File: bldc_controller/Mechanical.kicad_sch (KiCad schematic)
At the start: 9 parts

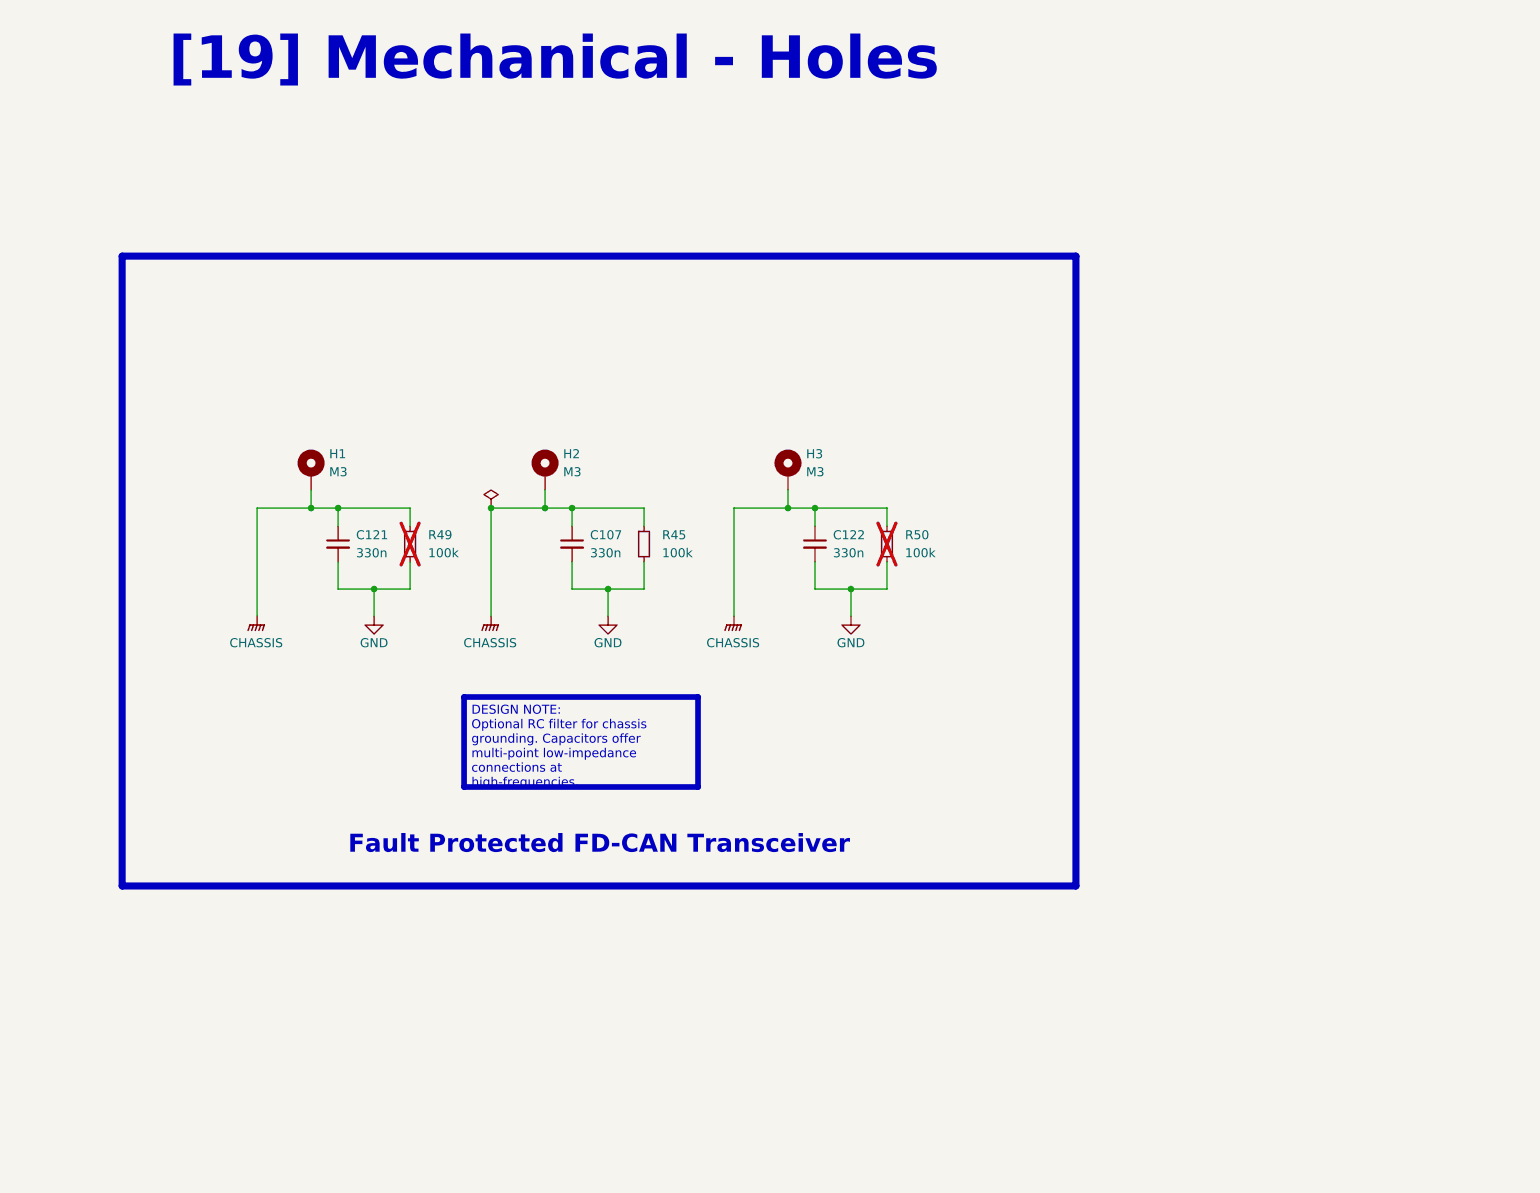
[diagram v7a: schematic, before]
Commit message: Replaced 3v3 buck with WSON package alternative. Will back-annotate components
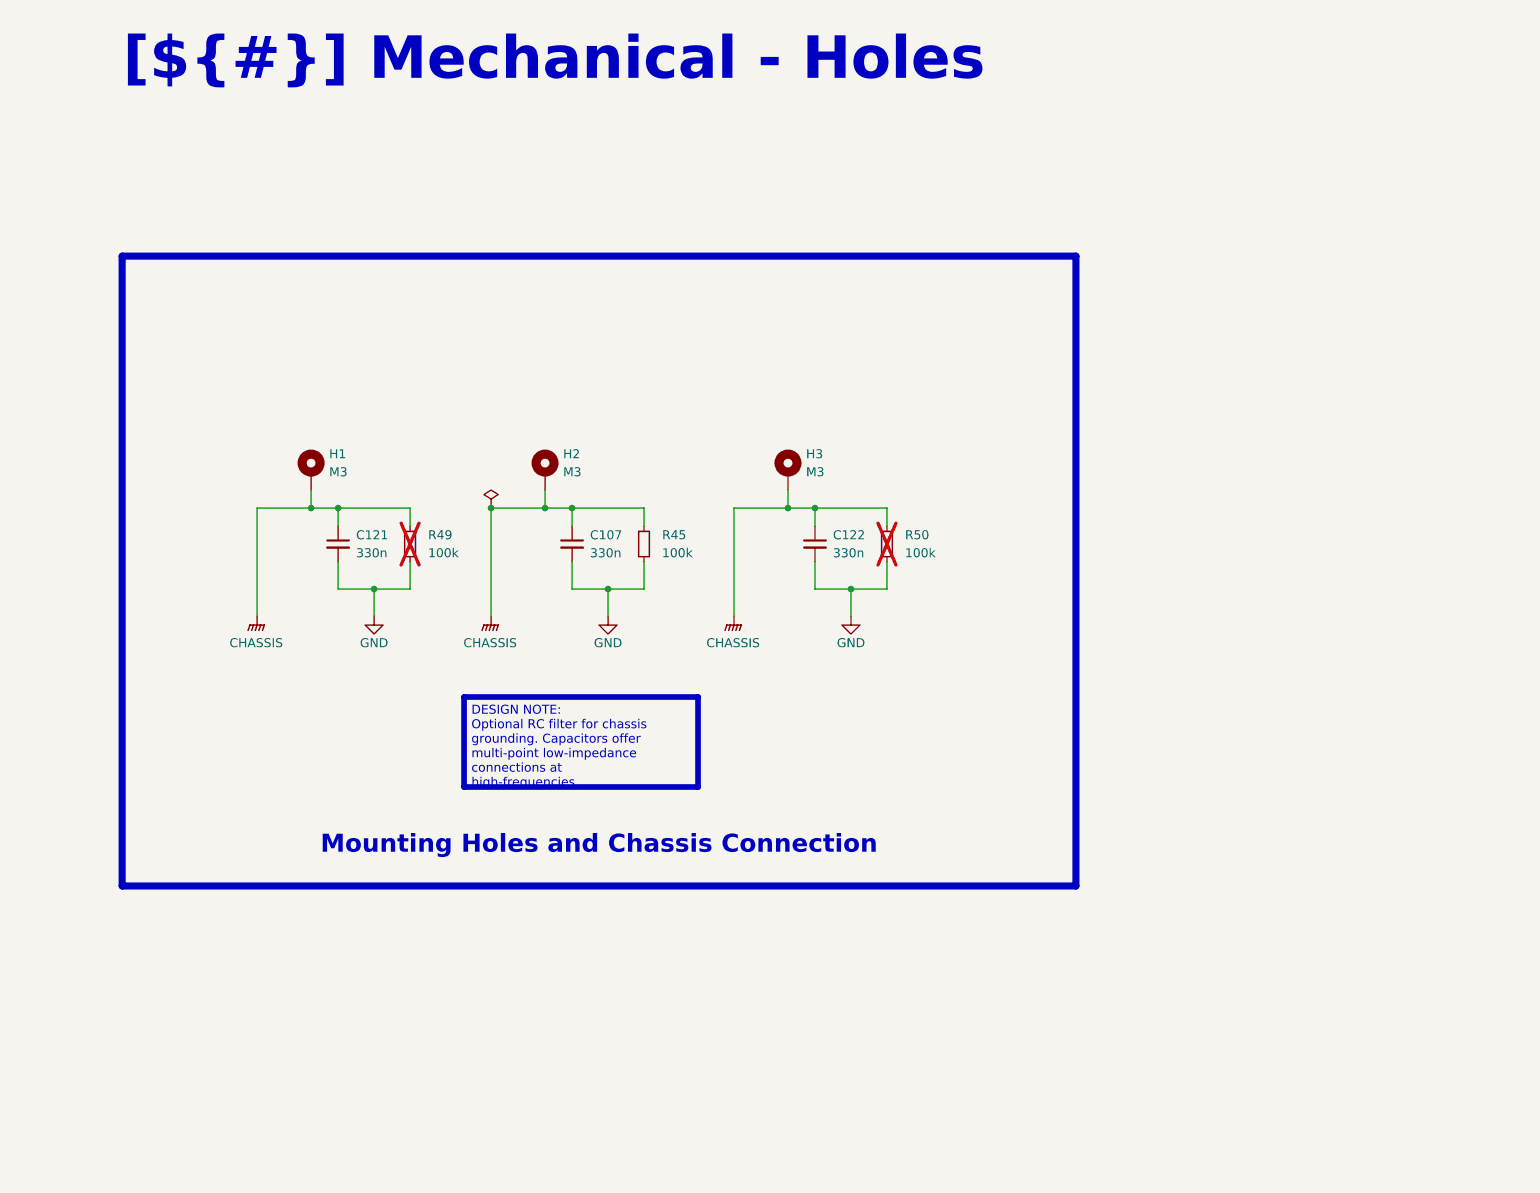
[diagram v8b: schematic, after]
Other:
- company: EPFL Xplore -> ${COMPANY}
- title: Mechanical Parts -> Mechanical - Holes
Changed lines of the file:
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@@
   (paper "A4")
   (title_block
-    (title "Mechanical Parts")
+    (title "Mechanical - Holes")
     (date "2023-10-22")
-    (rev "1.0")
-    (company "EPFL Xplore")
-    (comment 3 "Author: Vincent Nguyen")
+    (rev "${REVISION}")
+    (company "${COMPANY}")
+    (comment 3 "Author: ${AUTHOR}")
   )
-  (junction (at 189.23 97.79) (diameter 0) (color 0 0 0 1)
+  (junction (at 189.23 97.79) (diameter 0) (color 0 0 0 0)
   )
-  (junction (at 138.43 86.36) (diameter 0) (color 139 103 213 1)
+  (junction (at 138.43 86.36) (diameter 0) (color 0 0 0 0)
   )
-  (junction (at 146.05 86.36) (diameter 0) (color 139 103 213 1)
+  (junction (at 180.34 86.36) (diameter 0) (color 0 0 0 0)
   )
-  (junction (at 113.03 86.36) (diameter 0) (color 139 103 213 1)
+  (junction (at 113.03 86.36) (diameter 0) (color 0 0 0 0)
   )
-  (junction (at 154.94 97.79) (diameter 0) (color 0 0 0 1)
+  (junction (at 146.05 86.36) (diameter 0) (color 0 0 0 0)
   )
-  (junction (at 121.92 97.79) (diameter 0) (color 0 0 0 1)
+  (junction (at 154.94 97.79) (diameter 0) (color 0 0 0 0)
   )
-  (junction (at 180.34 86.36) (diameter 0) (color 139 103 213 1)
+  (junction (at 116.84 86.36) (diameter 0) (color 0 0 0 0)
   )
-  (junction (at 116.84 86.36) (diameter 0) (color 139 103 213 1)
+  (junction (at 184.15 86.36) (diameter 0) (color 0 0 0 0)
   )
-  (junction (at 149.86 86.36) (diameter 0) (color 139 103 213 1)
+  (junction (at 149.86 86.36) (diameter 0) (color 0 0 0 0)
   )
-  (junction (at 184.15 86.36) (diameter 0) (color 139 103 213 1)
+  (junction (at 121.92 97.79) (diameter 0) (color 0 0 0 0)
+  )
+  (wire (pts (xy 113.03 86.36) (xy 116.84 86.36))
+    (stroke (width 0) (type default))
   )
   (wire (pts (xy 184.15 97.79) (xy 189.23 97.79))
-    (stroke (width 0.381) (type default) (color 0 0 0 1))
+    (stroke (width 0) (type default))
+  )
+  (wire (pts (xy 127 97.79) (xy 127 93.98))
+    (stroke (width 0) (type default))
+  )
+  (wire (pts (xy 189.23 97.79) (xy 189.23 101.6))
+    (stroke (width 0) (type default))
+  )
+  (wire (pts (xy 184.15 86.36) (xy 184.15 88.9))
+    (stroke (width 0) (type default))
+  )
+  (wire (pts (xy 180.34 83.82) (xy 180.34 86.36))
+    (stroke (width 0) (type default))
+  )
+  (wire (pts (xy 172.72 86.36) (xy 180.34 86.36))
+    (stroke (width 0) (type default))
+  )
+  (wire (pts (xy 172.72 101.6) (xy 172.72 86.36))
+    (stroke (width 0) (type default))
+  )
+  (wire (pts (xy 160.02 86.36) (xy 160.02 88.9))
+    (stroke (width 0) (type default))
+  )
+  (wire (pts (xy 194.31 86.36) (xy 194.31 88.9))
+    (stroke (width 0) (type default))
+  )
+  (wire (pts (xy 116.84 93.98) (xy 116.84 97.79))
+    (stroke (width 0) (type default))
+  )
+  (wire (pts (xy 138.43 86.36) (xy 138.43 101.6))
+    (stroke (width 0) (type default))
+  )
+  (wire (pts (xy 149.86 86.36) (xy 160.02 86.36))
+    (stroke (width 0) (type default))
+  )
+  (wire (pts (xy 127 86.36) (xy 127 88.9))
+    (stroke (width 0) (type default))
+  )
+  (wire (pts (xy 105.41 86.36) (xy 113.03 86.36))
+    (stroke (width 0) (type default))
+  )
+  (wire (pts (xy 121.92 97.79) (xy 127 97.79))
+    (stroke (width 0) (type default))
+  )
+  (wire (pts (xy 154.94 97.79) (xy 160.02 97.79))
+    (stroke (width 0) (type default))
+  )
+  (wire (pts (xy 180.34 86.36) (xy 184.15 86.36))
+    (stroke (width 0) (type default))
+  )
+  (wire (pts (xy 160.02 97.79) (xy 160.02 93.98))
+    (stroke (width 0) (type default))
+  )
+  (wire (pts (xy 146.05 86.36) (xy 149.86 86.36))
+    (stroke (width 0) (type default))
   )
   (wire (pts (xy 146.05 83.82) (xy 146.05 86.36))
-    (stroke (width 0.381) (type default) (color 139 103 213 1))
+    (stroke (width 0) (type default))
   )
-  (wire (pts (xy 184.15 86.36) (xy 184.15 88.9))
-    (stroke (width 0.381) (type default) (color 139 103 213 1))
+  (wire (pts (xy 149.86 93.98) (xy 149.86 97.79))
+    (stroke (width 0) (type default))
   )
-  (wire (pts (xy 127 97.79) (xy 127 93.98))
-    (stroke (width 0.381) (type default) (color 0 0 0 1))
+  (wire (pts (xy 149.86 97.79) (xy 154.94 97.79))
+    (stroke (width 0) (type default))
   )
-  (wire (pts (xy 189.23 97.79) (xy 189.23 101.6))
-    (stroke (width 0.381) (type default) (color 0 0 0 1))
+  (wire (pts (xy 113.03 83.82) (xy 113.03 86.36))
+    (stroke (width 0) (type default))
+  )
+  (wire (pts (xy 194.31 97.79) (xy 194.31 93.98))
+    (stroke (width 0) (type default))
+  )
+  (wire (pts (xy 184.15 86.36) (xy 194.31 86.36))
+    (stroke (width 0) (type default))
+  )
+  (wire (pts (xy 149.86 86.36) (xy 149.86 88.9))
+    (stroke (width 0) (type default))
+  )
+  (wire (pts (xy 184.15 93.98) (xy 184.15 97.79))
+    (stroke (width 0) (type default))
+  )
+  (wire (pts (xy 116.84 86.36) (xy 116.84 88.9))
+    (stroke (width 0) (type default))
+  )
+  (wire (pts (xy 116.84 97.79) (xy 121.92 97.79))
+    (stroke (width 0) (type default))
+  )
+  (wire (pts (xy 116.84 86.36) (xy 127 86.36))
+    (stroke (width 0) (type default))
+  )
+  (wire (pts (xy 154.94 97.79) (xy 154.94 101.6))
+    (stroke (width 0) (type default))
+  )
+  (wire (pts (xy 121.92 97.79) (xy 121.92 101.6))
+    (stroke (width 0) (type default))
+  )
+  (wire (pts (xy 189.23 97.79) (xy 194.31 97.79))
+    (stroke (width 0) (type default))
+  )
+  (wire (pts (xy 138.43 86.36) (xy 146.05 86.36))
+    (stroke (width 0) (type default))
   )
   (wire (pts (xy 105.41 101.6) (xy 105.41 86.36))
-    (stroke (width 0.381) (type default) (color 139 103 213 1))
-  )
-  (wire (pts (xy 116.84 86.36) (xy 113.03 86.36))
-    (stroke (width 0.381) (type default) (color 139 103 213 1))
-  )
-  (wire (pts (xy 149.86 86.36) (xy 149.86 88.9))
-    (stroke (width 0.381) (type default) (color 139 103 213 1))
-  )
-  (wire (pts (xy 172.72 86.36) (xy 180.34 86.36))
-    (stroke (width 0.381) (type default) (color 139 103 213 1))
-  )
-  (wire (pts (xy 184.15 86.36) (xy 180.34 86.36))
-    (stroke (width 0.381) (type default) (color 139 103 213 1))
-  )
-  (wire (pts (xy 172.72 101.6) (xy 172.72 86.36))
-    (stroke (width 0.381) (type default) (color 139 103 213 1))
-  )
-  (wire (pts (xy 116.84 93.98) (xy 116.84 97.79))
-    (stroke (width 0.381) (type default) (color 0 0 0 1))
-  )
-  (wire (pts (xy 121.92 97.79) (xy 127 97.79))
-    (stroke (width 0.381) (type default) (color 0 0 0 1))
-  )
-  (wire (pts (xy 154.94 97.79) (xy 160.02 97.79))
-    (stroke (width 0.381) (type default) (color 0 0 0 1))
-  )
-  (wire (pts (xy 160.02 97.79) (xy 160.02 93.98))
-    (stroke (width 0.381) (type default) (color 0 0 0 1))
-  )
-  (wire (pts (xy 149.86 93.98) (xy 149.86 97.79))
-    (stroke (width 0.381) (type default) (color 0 0 0 1))
-  )
-  (wire (pts (xy 127 86.36) (xy 116.84 86.36))
-    (stroke (width 0.381) (type default) (color 139 103 213 1))
-  )
-  (wire (pts (xy 149.86 97.79) (xy 154.94 97.79))
-    (stroke (width 0.381) (type default) (color 0 0 0 1))
-  )
-  (wire (pts (xy 105.41 86.36) (xy 113.03 86.36))
-    (stroke (width 0.381) (type default) (color 139 103 213 1))
-  )
-  (wire (pts (xy 160.02 86.36) (xy 149.86 86.36))
-    (stroke (width 0.381) (type default) (color 139 103 213 1))
-  )
-  (wire (pts (xy 180.34 83.82) (xy 180.34 86.36))
-    (stroke (width 0.381) (type default) (color 139 103 213 1))
-  )
-  (wire (pts (xy 194.31 97.79) (xy 194.31 93.98))
-    (stroke (width 0.381) (type default) (color 0 0 0 1))
-  )
-  (wire (pts (xy 138.43 101.6) (xy 138.43 86.36))
-    (stroke (width 0.381) (type default) (color 139 103 213 1))
-  )
-  (wire (pts (xy 184.15 93.98) (xy 184.15 97.79))
-    (stroke (width 0.381) (type default) (color 0 0 0 1))
-  )
-  (wire (pts (xy 149.86 86.36) (xy 146.05 86.36))
-    (stroke (width 0.381) (type default) (color 139 103 213 1))
-  )
-  (wire (pts (xy 116.84 97.79) (xy 121.92 97.79))
-    (stroke (width 0.381) (type default) (color 0 0 0 1))
-  )
-  (wire (pts (xy 154.94 97.79) (xy 154.94 101.6))
-    (stroke (width 0.381) (type default) (color 0 0 0 1))
-  )
-  (wire (pts (xy 121.92 97.79) (xy 121.92 101.6))
-    (stroke (width 0.381) (type default) (color 0 0 0 1))
-  )
-  (wire (pts (xy 189.23 97.79) (xy 194.31 97.79))
-    (stroke (width 0.381) (type default) (color 0 0 0 1))
-  )
-  (wire (pts (xy 194.31 86.36) (xy 184.15 86.36))
-    (stroke (width 0.381) (type default) (color 139 103 213 1))
-  )
-  (wire (pts (xy 116.84 86.36) (xy 116.84 88.9))
-    (stroke (width 0.381) (type default) (color 139 103 213 1))
-  )
-  (wire (pts (xy 113.03 83.82) (xy 113.03 86.36))
-    (stroke (width 0.381) (type default) (color 139 103 213 1))
-  )
-  (wire (pts (xy 138.43 86.36) (xy 146.05 86.36))
-    (stroke (width 0.381) (type default) (color 139 103 213 1))
-  )
-  (wire (pts (xy 194.31 88.9) (xy 194.31 86.36))
-    (stroke (width 0.381) (type default) (color 139 103 213 1))
-  )
-  (wire (pts (xy 127 88.9) (xy 127 86.36))
-    (stroke (width 0.381) (type default) (color 139 103 213 1))
-  )
-  (wire (pts (xy 160.02 88.9) (xy 160.02 86.36))
-    (stroke (width 0.381) (type default) (color 139 103 213 1))
+    (stroke (width 0) (type default))
   )
   (rectangle (start 86.36 50.8) (end 220.98 139.7)
@@
     (fill (type none))
   )
-  (text_box "[19] Mechanical - Holes"
+  (text_box "[${#}] ${TITLE}"
     (at 78.74 16.51 0) (size 137.16 12.7)
     (stroke (width -0.0001) (type default))
@@
     (effects (font (face "Times New Roman") (size 6 6) (thickness 1.2) bold (color 162 22 34 1)))
   )
-  (text_box "Fault Protected FD-CAN Transceiver"
+  (text_box "Mounting Holes and Chassis Connection"
     (at 87.63 128.27 0) (size 132.08 8.89)
     (stroke (width -0.0001) (type default))
